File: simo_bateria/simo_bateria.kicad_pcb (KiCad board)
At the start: 2 copper layers, 23 x 88 mm, 4 parts, among them J1 conector salida, U1 simo_bateria, U2 cargador_bateria, U3 conversor_dc

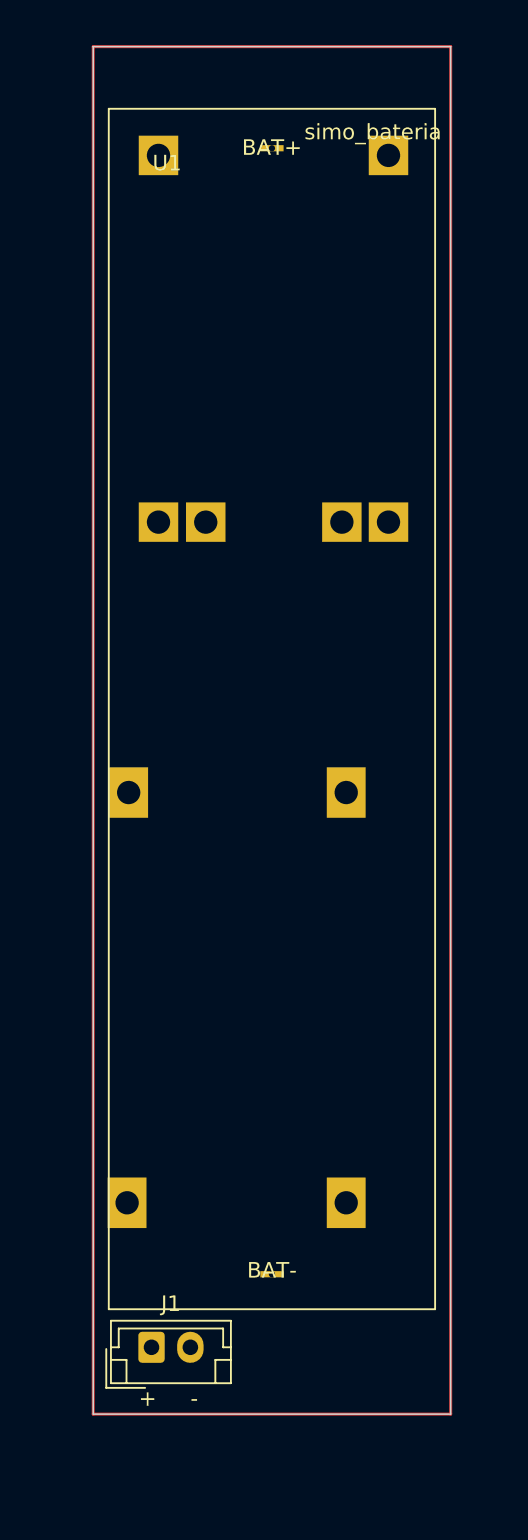
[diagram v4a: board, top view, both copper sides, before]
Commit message: update, se corrijio imagen step de simo_bateria
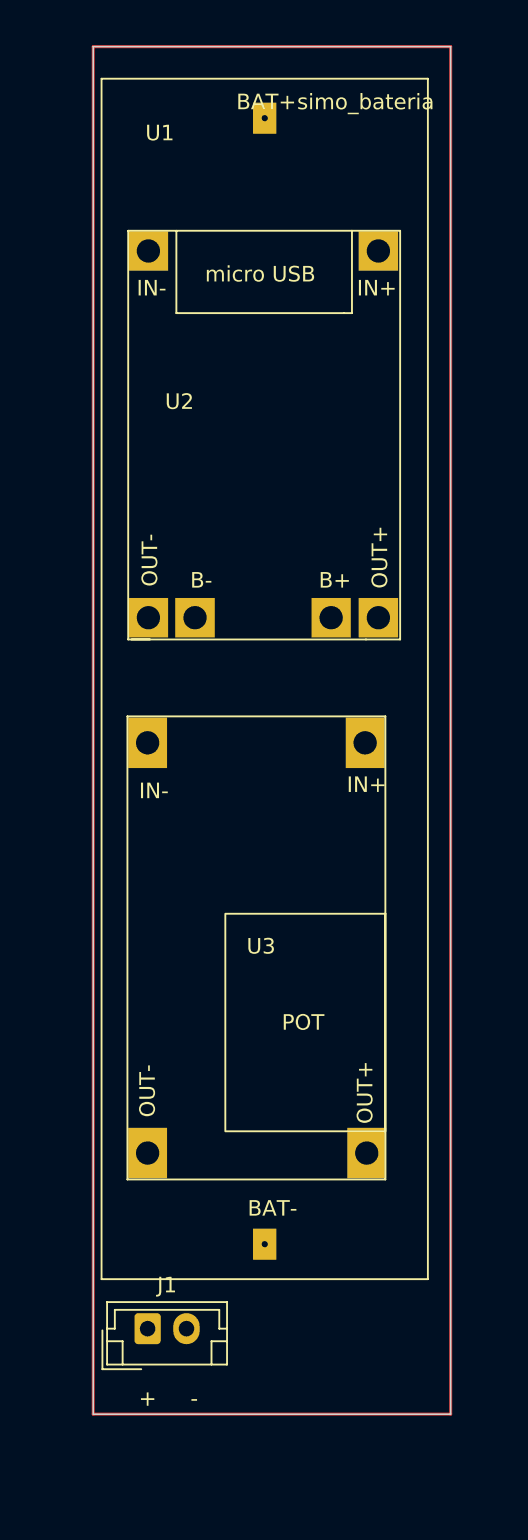
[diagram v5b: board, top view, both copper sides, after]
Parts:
- U2, U3: moved to F.Cu
- moved U2 16.6 mm to (122.5, 39.1), turned to 0 degrees
- moved U3 13.2 mm to (122.5, 70.8), turned to 0 degrees
- moved U1 1.99 mm to (130.0, 28.1)
- moved J1 1.23 mm to (122.5, 108.5)

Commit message: simo_bateria
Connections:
- net Net-(J1-Pad1) renamed +3V3
- net Net-(J1-Pad2) renamed GND
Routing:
- net Net-(U1-Pad2): track 0.00 -> 51.1 mm
- net Net-(U1-Pad1): track 0.00 -> 35.2 mm
- net +3V3: track 0.00 -> 27.7 mm
- net GND: track 0.00 -> 12.3 mm
- net Net-(U2-Pad3): track 0.00 -> 9.31 mm
- net Net-(U2-Pad5): track 0.00 -> 8.96 mm
- added copper zone on F.Cu, net GND
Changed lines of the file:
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@@
   )
   (setup
+    (stackup
+      (layer "F.SilkS" (type "Top Silk Screen"))
+      (layer "F.Paste" (type "Top Solder Paste"))
+      (layer "F.Mask" (type "Top Solder Mask") (thickness 0.01))
+      (layer "F.Cu" (type "copper") (thickness 0.035))
+      (layer "dielectric 1" (type "core") (thickness 1.51) (material "FR4") (epsilon_r 4.5) (loss_tangent 0.02))
+      (layer "B.Cu" (type "copper") (thickness 0.035))
+      (layer "B.Mask" (type "Bottom Solder Mask") (thickness 0.01))
+      (layer "B.Paste" (type "Bottom Solder Paste"))
+      (layer "B.SilkS" (type "Bottom Silk Screen"))
+      (copper_finish "None")
+      (dielectric_constraints no)
+    )
     (pad_to_mask_clearance 0)
     (pcbplotparams
@@
   (net 5 "unconnected-(U2-Pad4)")
   (net 6 "Net-(U2-Pad5)")
-  (net 7 "Net-(J1-Pad1)")
-  (net 8 "Net-(J1-Pad2)")
+  (net 7 "GND")
+  (net 8 "+3V3")
   (footprint "Connector_JST:JST_EH_B2B-EH-A_1x02_P2.50mm_Vertical" (layer "F.Cu")
     (at 122.5 108.5)
@@
     (fp_line (start -2.5 -1.6) (end -2.5 2.2) (layer "F.Fab") (width 0.1))
     (pad "1" thru_hole roundrect (at 0 0) (size 1.7 2) (drill 1) (layers *.Cu *.Mask) (roundrect_rratio 0.147059)
-      (net 7 "Net-(J1-Pad1)") (pinfunction "Pin_1") (pintype "passive"))
+      (net 8 "+3V3") (pinfunction "Pin_1") (pintype "passive"))
     (pad "2" thru_hole oval (at 2.5 0) (size 1.7 2) (drill 1) (layers *.Cu *.Mask)
-      (net 8 "Net-(J1-Pad2)") (pinfunction "Pin_2") (pintype "passive"))
+      (net 7 "GND") (pinfunction "Pin_2") (pintype "passive"))
     (model "/home/gvelardez/simo_pcb/proyecto_definitivo/simo_pcb/simo_pcb/simo/otros/JST-B2B-EH-A.STEP"
       (offset (xyz 0 0 0))
@@
       (net 4 "Net-(U2-Pad3)") (pinfunction "VIN-") (pintype "input"))
     (pad "2" thru_hole rect (at 0 26.4) (size 2.5 3.25) (drill 1.5) (layers *.Cu *.Mask)
-      (net 8 "Net-(J1-Pad2)") (pinfunction "VOUT-") (pintype "power_out"))
+      (net 7 "GND") (pinfunction "VOUT-") (pintype "power_out"))
     (pad "3" thru_hole rect (at 14 0) (size 2.5 3.25) (drill 1.5) (layers *.Cu *.Mask)
       (net 6 "Net-(U2-Pad5)") (pinfunction "VIN+") (pintype "power_in"))
     (pad "4" thru_hole rect (at 14.1 26.4) (size 2.5 3.25) (drill 1.5) (layers *.Cu *.Mask)
-      (net 7 "Net-(J1-Pad1)") (pinfunction "VOUT+") (pintype "power_in"))
+      (net 8 "+3V3") (pinfunction "VOUT+") (pintype "power_in"))
     (model "/home/gvelardez/simo_pcb/proyecto_definitivo/simo_pcb/simo_pcb/simo/otros/conversor/MT3608 Converter.STEP"
       (offset (xyz 7 -13 0))
@@
     (effects (font (size 1 1) (thickness 0.15)))
   )
+  (segment (start 130.035 49.035) (end 137.35 56.35) (width 1) (layer "F.Cu") (net 1))
+  (segment (start 130.035 30.605) (end 130.035 49.035) (width 1) (layer "F.Cu") (net 1))
+  (segment (start 137.35 56.35) (end 137.35 62.75) (width 1) (layer "F.Cu") (net 1))
+  (segment (start 130.035 103.065) (end 130.035 63.295978) (width 1) (layer "F.Cu") (net 2))
+  (segment (start 126.739022 60) (end 123 60) (width 1) (layer "F.Cu") (net 2))
+  (segment (start 130.035 63.295978) (end 126.739022 60) (width 1) (layer "F.Cu") (net 2))
+  (segment (start 122.55 60.45) (end 122.55 62.75) (width 1) (layer "F.Cu") (net 2))
+  (segment (start 123 60) (end 122.55 60.45) (width 1) (layer "F.Cu") (net 2))
+  (segment (start 125.55 67.75) (end 125.55 62.75) (width 1) (layer "F.Cu") (net 4))
+  (segment (start 122.5 70.8) (end 125.55 67.75) (width 1) (layer "F.Cu") (net 4))
+  (segment (start 134.31 68.61) (end 134.31 62.75) (width 1) (layer "F.Cu") (net 6))
+  (segment (start 136.5 70.8) (end 134.31 68.61) (width 1) (layer "F.Cu") (net 6))
+  (segment (start 125 108.5) (end 125 99.7) (width 1) (layer "F.Cu") (net 7))
+  (segment (start 125 99.7) (end 122.5 97.2) (width 1) (layer "F.Cu") (net 7))
+  (segment (start 123 109) (end 123 112) (width 1) (layer "F.Cu") (net 8))
+  (segment (start 122.5 108.5) (end 123 109) (width 1) (layer "F.Cu") (net 8))
+  (segment (start 123 112) (end 129 112) (width 1) (layer "F.Cu") (net 8))
+  (segment (start 129 112) (end 136.6 104.4) (width 1) (layer "F.Cu") (net 8))
+  (segment (start 136.6 104.4) (end 136.6 97.2) (width 1) (layer "F.Cu") (net 8))
+  (zone (net 7) (net_name "GND") (layer "F.Cu") (hatch edge 0.508)
+    (connect_pads (clearance 0))
+    (min_thickness 0.254) (filled_areas_thickness no)
+    (fill yes (thermal_gap 0.508) (thermal_bridge_width 0.508))
+    (polygon
+      (pts
+        (xy 145 115)
+        (xy 115 115)
+        (xy 115 25)
+        (xy 145 25)
+      )
+    )
+  )
 )

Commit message: se actualizo la placa bateria
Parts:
- removed U1: simo_bateria, simo_bateria:bateria
- added BAT1: bateria, Battery:BatteryHolder_MPD_BH-18650-PC2, F.Cu at (130.0, 31.0)
- J1, U2, U3: moved to B.Cu
- moved U2 15.3 mm to (137.4, 35.6), turned to 180 degrees
- moved U3 15.0 mm to (137.0, 67.0), turned to 180 degrees
- moved J1 1.50 mm to (122.5, 110.0)
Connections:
- J1 pad 1: +3V3 -> +BATT
- U3 pad 1: Net-(U2-Pad3) -> Net-(U2-Pad5)
- U3 pad 2: GND -> +BATT
- U3 pad 3: Net-(U2-Pad5) -> Net-(U2-Pad3)
- U3 pad 4: +3V3 -> GND
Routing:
- net +BATT: track 0.00 -> 32.0 mm
- net +3V3: track 27.7 -> 0.00 mm
- net Net-(U2-Pad5): track 8.96 -> 27.5 mm
- net Net-(U2-Pad3): track 9.31 -> 14.7 mm
- net GND: track 12.3 -> 17.5 mm
- net Net-(BAT1-Pad2): track 51.1 -> 46.8 mm
- net Net-(BAT1-Pad1): track 35.2 -> 31.3 mm
- added copper zone on B.Cu, net GND
- removed copper zone on F.Cu, net GND
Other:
- board size 23 x 88 mm -> 24 x 88 mm

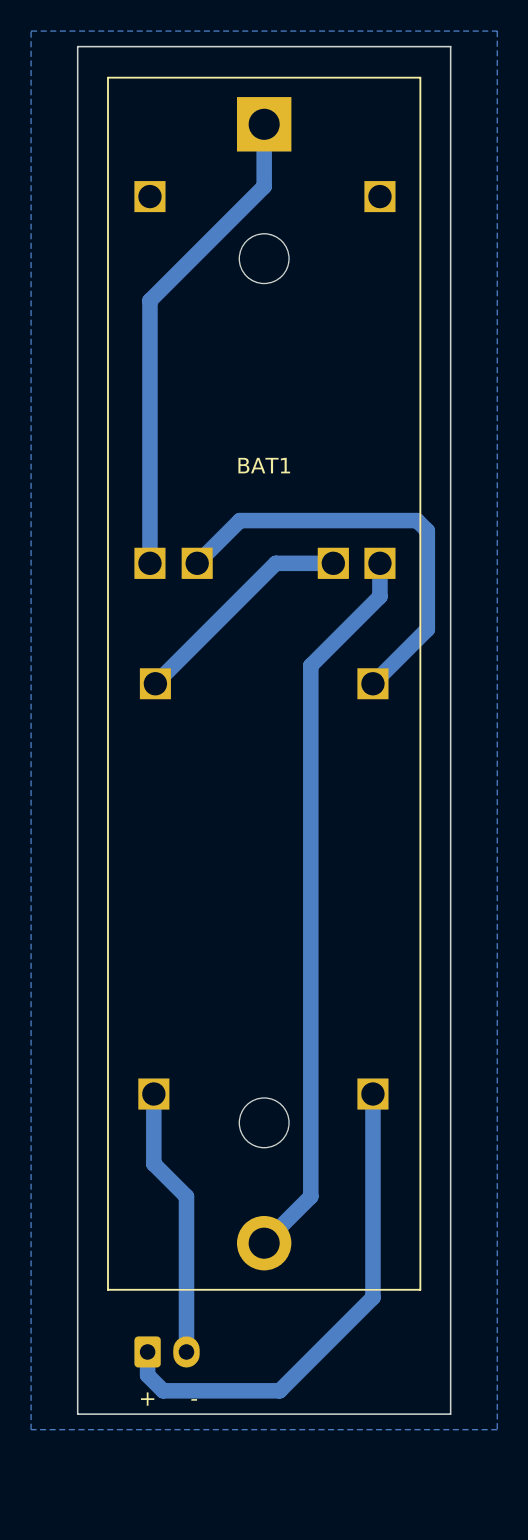
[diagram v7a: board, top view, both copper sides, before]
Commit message: se agrego un circuito para mediciones de tension de bateria mediante la bluepill
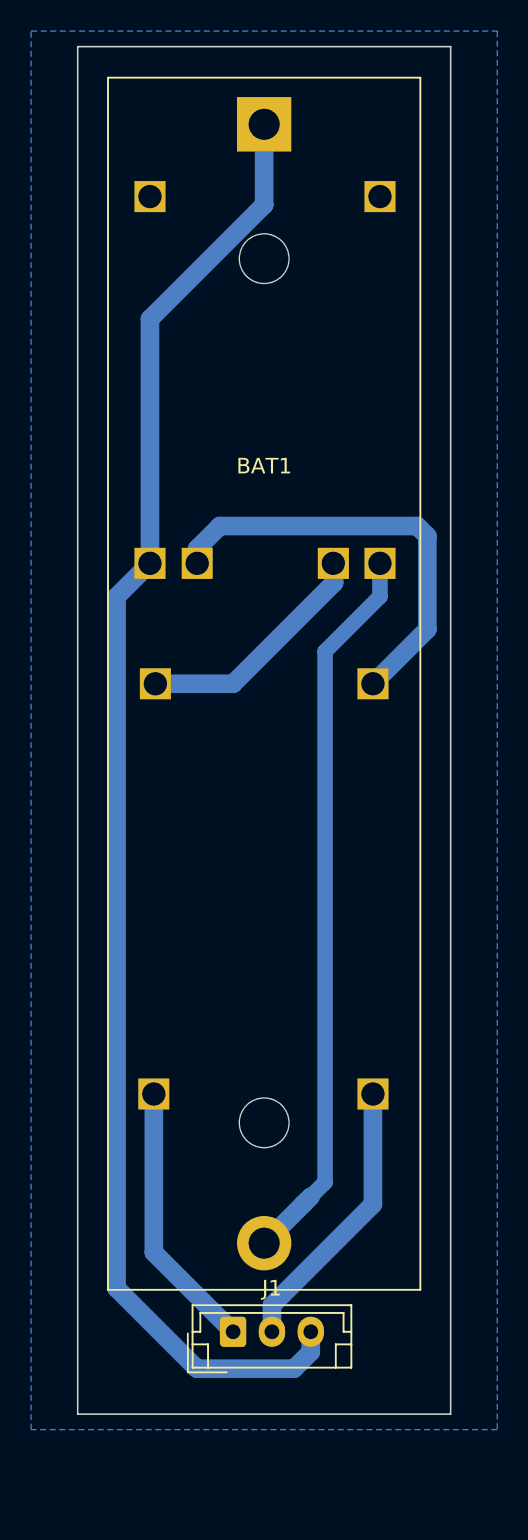
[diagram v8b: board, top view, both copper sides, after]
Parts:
- J1: value conector salida -> CONECTOR SALIDA; footprint Connector_JST:JST_EH_B2B-EH-A_1x02_P2.50mm_Vertical -> Connector_JST:JST_EH_B3B-EH-A_1x03_P2.50mm_Vertical; moved to F.Cu
- moved J1 5.65 mm to (128.0, 108.7)
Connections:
- U3 pad 2: +BATT -> GND
- U3 pad 4: GND -> +BATT
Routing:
- net Net-(BAT1-Pad1): track 31.3 -> 99.2 mm
- net +BATT: track 32.0 -> 17.4 mm
- net Net-(U2-Pad3): track 14.7 -> 15.5 mm
- net Net-(BAT1-Pad2): track 46.8 -> 47.5 mm
- net GND: track 17.5 -> 18.0 mm
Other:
- board text removed: "+"
- board text removed: "-"
